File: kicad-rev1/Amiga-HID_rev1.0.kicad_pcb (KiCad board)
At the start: 4 copper layers, 20 x 55 mm, 57 parts, among them J1 USB-A Host, J2 JST-XH-5A, J3 OLED I2C, J4 Reserve 3V3+GP+GND+VSYS, J5 JST-SH-3 SWD, J6 JST-SH-3 UART, J7 Conn_01x06_Pin, SW1 SW_Push, SW2 SW_Push, U1 USBLC6-2SC6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

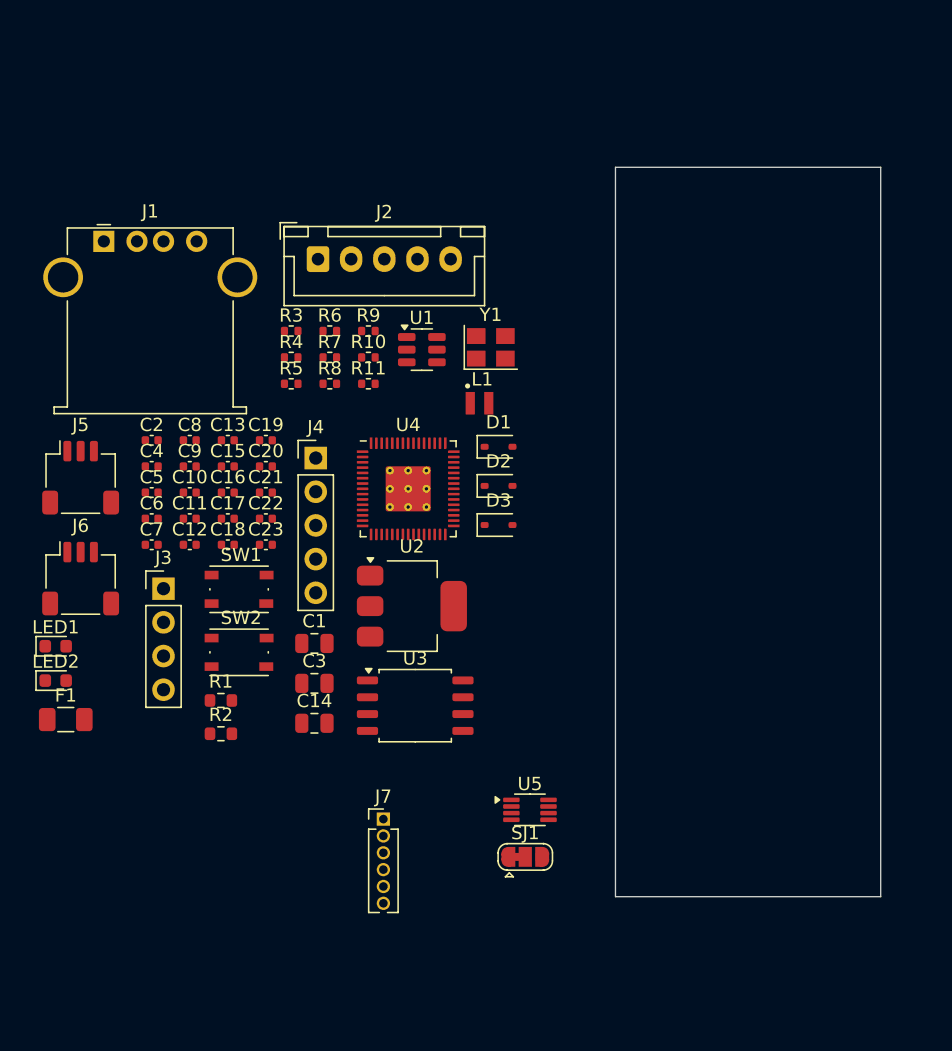
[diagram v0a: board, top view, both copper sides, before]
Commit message: korrekte USB-A Buchse
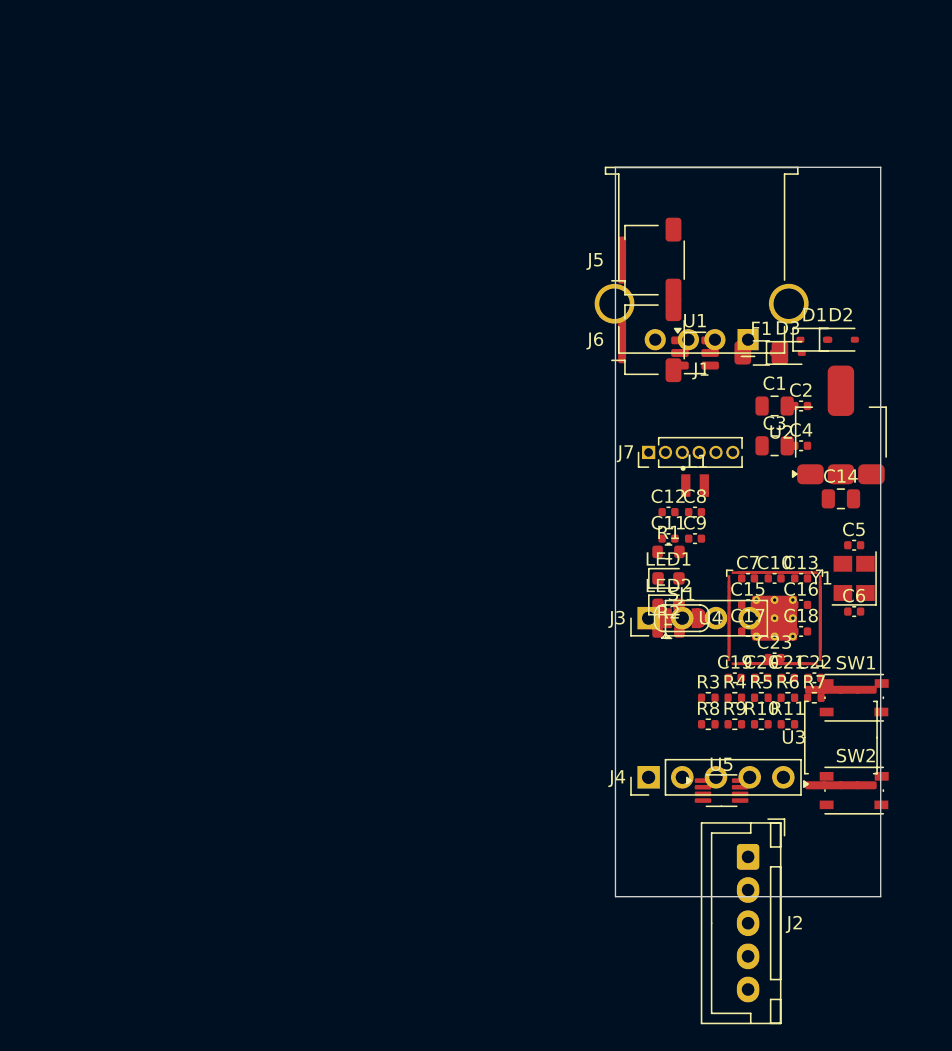
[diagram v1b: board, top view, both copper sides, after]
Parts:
- C10, C13, C15, C16, C17, C18, C23, C7: moved to B.Cu
- J1: footprint Connector_USB:USB_A_Stewart_SS-52100-001_Horizontal -> Amiga-HID_rev1.0:USB_A_Receptacle_Edge_C42614
- moved F1 59.3 mm to (161.0, 114.0)
- moved J2 55.5 mm to (160.0, 152.0), turned to 270 degrees
- moved C6 53.4 mm to (168.0, 133.5)
- moved C5 53.1 mm to (168.0, 128.5)
- moved J1 49.1 mm to (160.0, 113.0), turned to 180 degrees
- moved C2 49.0 mm to (164.0, 118.0)
- moved C4 49.0 mm to (164.0, 121.0)
- moved SW2 47.5 mm to (168.0, 147.0)
- moved SW1 47.1 mm to (168.0, 140.0)
- moved LED2 46.6 mm to (154.0, 133.0)
- moved LED1 46.5 mm to (154.0, 131.0)
- moved J6 46.5 mm to (152.5, 113.0), turned to 90 degrees
- moved J5 45.9 mm to (152.5, 107.0), turned to 90 degrees
- moved C7 45.0 mm to (160.0, 131.0)
- moved R7 44.7 mm to (165.0, 140.0)
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
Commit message: alle 3d modelle implementiert
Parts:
- SW1, SW2: footprint Button_Switch_SMD:SW_Push_1P1T_NO_Vertical_Wuerth_434133025816 -> Amiga-HID_rev1.0:SW_SMD_Tact_4x3_4P_C139797
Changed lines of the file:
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@@
 	(net 65 "/GPIO24")
 	(net 66 "/GPIO23")
-	(footprint "Button_Switch_SMD:SW_Push_1P1T_NO_Vertical_Wuerth_434133025816"
+	(footprint "Amiga-HID_rev1.0:SW_SMD_Tact_4x3_4P_C139797"
 		(layer "F.Cu")
 		(at 168 140)
@@
 			)
 		)
-		(property "Footprint" "Button_Switch_SMD:SW_Push_1P1T_NO_Vertical_Wuerth_434133025816"
+		(property "Footprint" "Amiga-HID_rev1.0:SW_SMD_Tact_4x3_4P_C139797"
 			(at 0 0 0)
 			(unlocked yes)
@@
 			(pintype "passive")
 		)
-		(model "${KICAD8_3DMODEL_DIR}/Button_Switch_SMD.3dshapes/SW_Push_1P1T_NO_Vertical_Wuerth_434133025816.wrl"
+		(model "${KIPRJMOD}/Amiga-HID_rev1.0.pretty/3d/C139797_TactSwitch_4x3.wrl"
 			(offset
 				(xyz 0 0 0)
@@
 			(pintype "passive")
 		)
-		(model "${KICAD7_3DMODEL_DIR}/Inductor_SMD.3dshapes/AOTA-B201610SR47MT.STEP"
+		(model "${KIPRJMOD}/Amiga-HID_rev1.0.pretty/3d/C1046_Sunlord_L_0805_2u2.wrl"
 			(offset
-				(xyz 0 0 0.5)
+				(xyz 0 0 0)
 			)
 			(scale
@@
 			)
 			(rotate
-				(xyz -90 0 0)
+				(xyz 0 0 0)
 			)
 		)
@@
 			(roundrect_rratio 0.208333)
 		)
-		(model "${KICAD8_3DMODEL_DIR}/Connector_JST.3dshapes/JST_SH_SM03B-SRSS-TB_1x03-1MP_P1.00mm_Horizontal.wrl"
+		(model "${KIPRJMOD}/Amiga-HID_rev1.0.pretty/3d/C160403_JST_SH_SM03B-SRSS-TB.wrl"
 			(offset
 				(xyz 0 0 0)
@@
 			(roundrect_rratio 0.208333)
 		)
-		(model "${KICAD8_3DMODEL_DIR}/Connector_JST.3dshapes/JST_SH_SM03B-SRSS-TB_1x03-1MP_P1.00mm_Horizontal.wrl"
+		(model "${KIPRJMOD}/Amiga-HID_rev1.0.pretty/3d/C160403_JST_SH_SM03B-SRSS-TB.wrl"
 			(offset
 				(xyz 0 0 0)
@@
 			(pintype "passive")
 		)
-		(model "${KICAD8_3DMODEL_DIR}/Connector_USB.3dshapes/USB_A_Stewart_SS-52100-001_Horizontal.wrl"
+		(model "${KIPRJMOD}/Amiga-HID_rev1.0.pretty/3d/C42614_USB-A-TH_JTJ.wrl"
 			(offset
 				(xyz 0 0 0)
@@
 		)
 	)
-	(footprint "Button_Switch_SMD:SW_Push_1P1T_NO_Vertical_Wuerth_434133025816"
+	(footprint "Amiga-HID_rev1.0:SW_SMD_Tact_4x3_4P_C139797"
 		(layer "F.Cu")
 		(at 168 147)
@@
 			)
 		)
-		(property "Footprint" "Button_Switch_SMD:SW_Push_1P1T_NO_Vertical_Wuerth_434133025816"
+		(property "Footprint" "Amiga-HID_rev1.0:SW_SMD_Tact_4x3_4P_C139797"
 			(at 0 0 0)
 			(unlocked yes)
@@
 			(pintype "passive")
 		)
-		(model "${KICAD8_3DMODEL_DIR}/Button_Switch_SMD.3dshapes/SW_Push_1P1T_NO_Vertical_Wuerth_434133025816.wrl"
+		(model "${KIPRJMOD}/Amiga-HID_rev1.0.pretty/3d/C139797_TactSwitch_4x3.wrl"
 			(offset
 				(xyz 0 0 0)

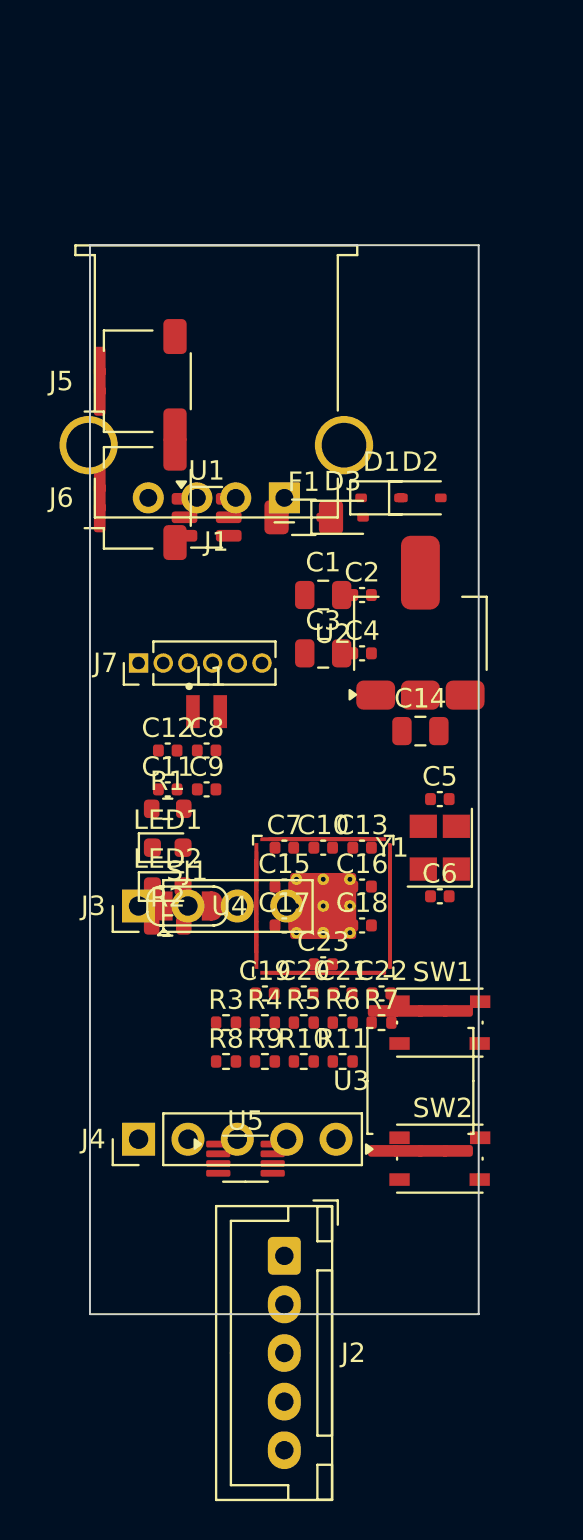
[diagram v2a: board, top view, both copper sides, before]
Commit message: aufteilung Bauteile Vorder und Rückseite
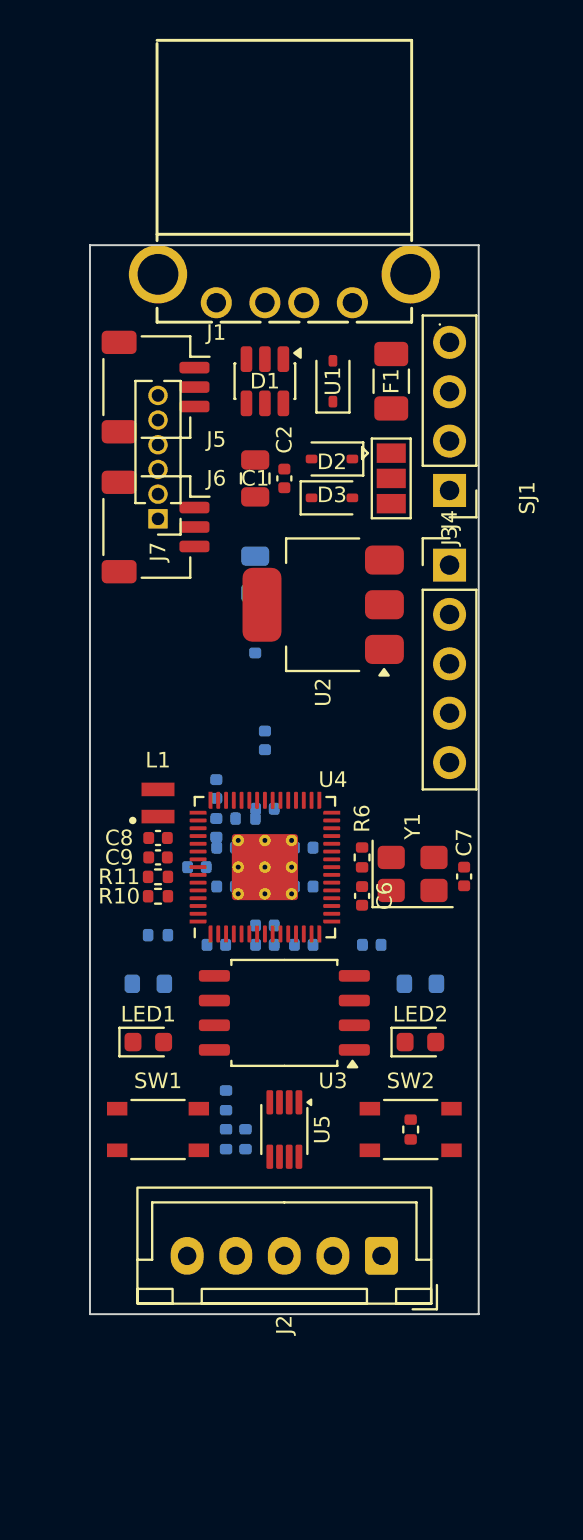
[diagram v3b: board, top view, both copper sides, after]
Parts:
- removed C14: 10u, Capacitor_SMD:C_0805_2012Metric
- C10: renamed from C11; moved to B.Cu
- C12, C19, C20, C3, C4, R1, R2, R3, R4, R5, R8, R9: moved to B.Cu
- C21: renamed from C22; moved to B.Cu
- C22: renamed from C21; moved to B.Cu
- SJ1: footprint Jumper:SolderJumper-3_P1.3mm_Bridged12_RoundedPad1.0x1.5mm -> Jumper:SolderJumper-3_P1.3mm_Open_Pad1.0x1.5mm
- U3: footprint Package_SO:SOIC-8_5.23x5.23mm_P1.27mm -> Amiga-HID_rev1.0:SOIC-8_5.3x5.3mm_P1.27mm
- moved J4 33.6 mm to (168.5, 116.5), turned to 0 degrees
- moved J3 26.7 mm to (168.5, 112.6), turned to 180 degrees
- moved SJ1 24.4 mm to (165.5, 112.0), turned to -90 degrees
- moved SW1 15.5 mm to (153.5, 145.5)
- moved LED2 15.3 mm to (167.0, 141.0)
- moved R11 13.4 mm to (153.5, 132.5)
- moved R2 13.3 mm to (167.0, 138.0)
- moved R8 12.5 mm to (158.0, 129.5)
- moved R10 11.3 mm to (153.5, 133.5)
- moved J1 10.8 mm to (160.0, 102.2)
- moved LED1 10.0 mm to (153.0, 141.0)
- moved R1 9.06 mm to (153.0, 138.0)
- moved C13 8.56 mm to (155.5, 132.0)
- moved R6 8.56 mm to (164.0, 131.5), turned to 90 degrees
- moved F1 8.32 mm to (165.5, 107.0), turned to 90 degrees
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- renumbered C10 to C11, C7 to C5, C5 to C6, C6 to C7

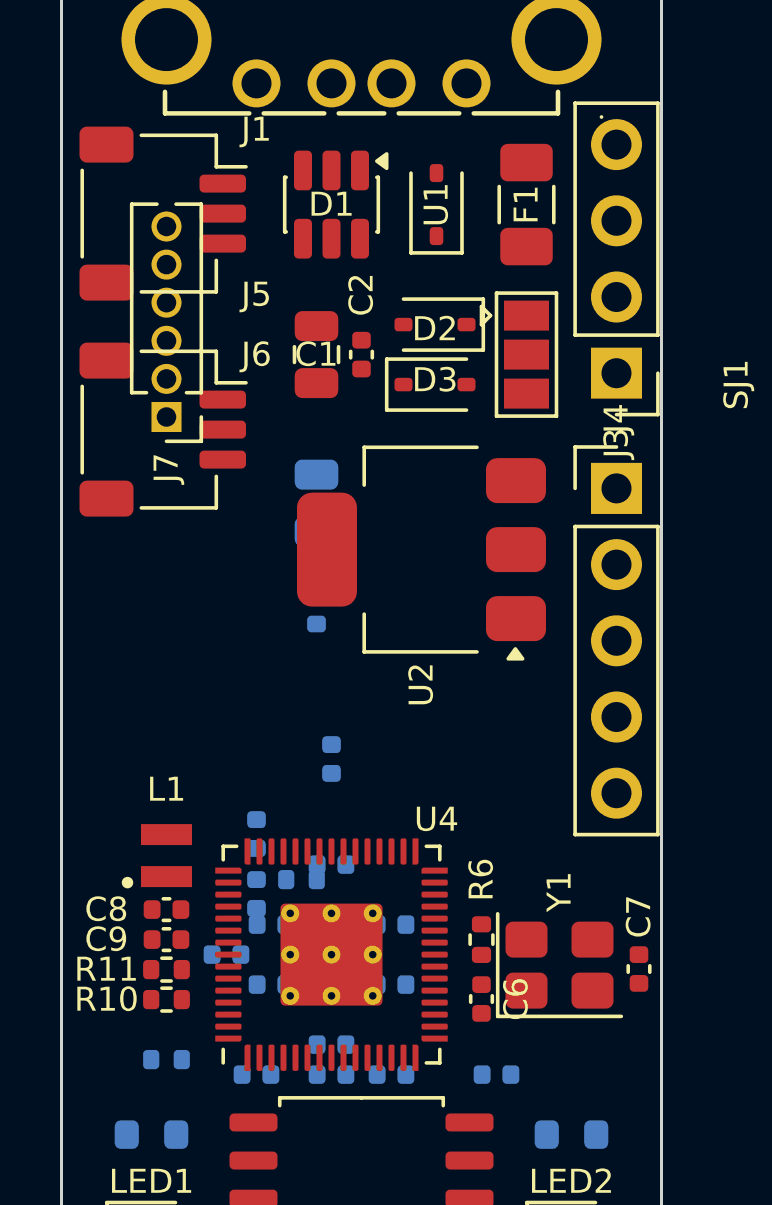
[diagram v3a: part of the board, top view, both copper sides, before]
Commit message: Wiederstände überarbeitet
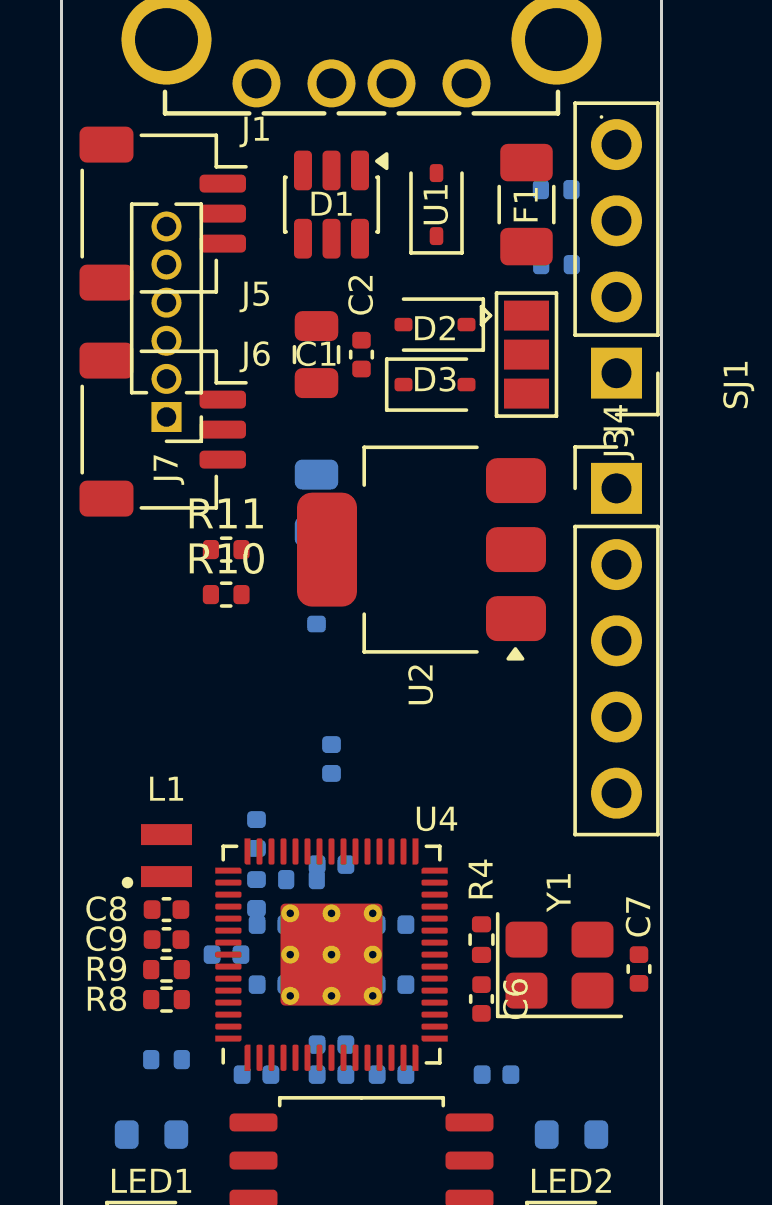
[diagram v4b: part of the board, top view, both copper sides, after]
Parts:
- added R10: 33, Resistor_SMD:R_0402_1005Metric, F.Cu at (155.5, 120.0)
- added R11: 33, Resistor_SMD:R_0402_1005Metric, F.Cu at (155.5, 118.5)
- added R12: DNF, Resistor_SMD:R_0402_1005Metric, B.Cu at (166.5, 109.0)
- added R13: DNF, Resistor_SMD:R_0402_1005Metric, B.Cu at (166.5, 106.5)
- R3: renamed from R5; value DNF -> 10k
- U3: value W25Q128JVS -> W25Q16JVSSIQ
- renumbered R6 to R4, R8 to R5, R9 to R6, R10 to R8, R11 to R9
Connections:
- R3 pad 2: /FLASH_SS -> /QSPI_SS
- U3 pad 1: /FLASH_SS -> /QSPI_SS
- U4 pad 2: /UART_TX -> Net-(U4-GPIO0)
- U4 pad 3: /UART_RX -> Net-(U4-GPIO1)
